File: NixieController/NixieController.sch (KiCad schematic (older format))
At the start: 87 parts, among them J1 Conn_02x05_Odd_Even, J10 Conn_01x06, J11 Conn_01x05, J12 Barrel_Jack, J13 Conn_02x05_Odd_Even, J14 Conn_02x05_Odd_Even, J15 Conn_02x05_Odd_Even, J16 Conn_01x07, J17 Conn_01x04, J18 Conn_01x02, J2 Conn_01x01, J3 Conn_01x01, J4 Conn_01x01, J5 Conn_01x01, J6 Conn_01x04, J8 Conn_01x04, Q1 2N2222A, Q2 2N2222A, Q3 2N2222A, Q4 2N2222A, SW1 SW_Push, SW2 SW_Push, SW3 SW_Push, U2 L7805

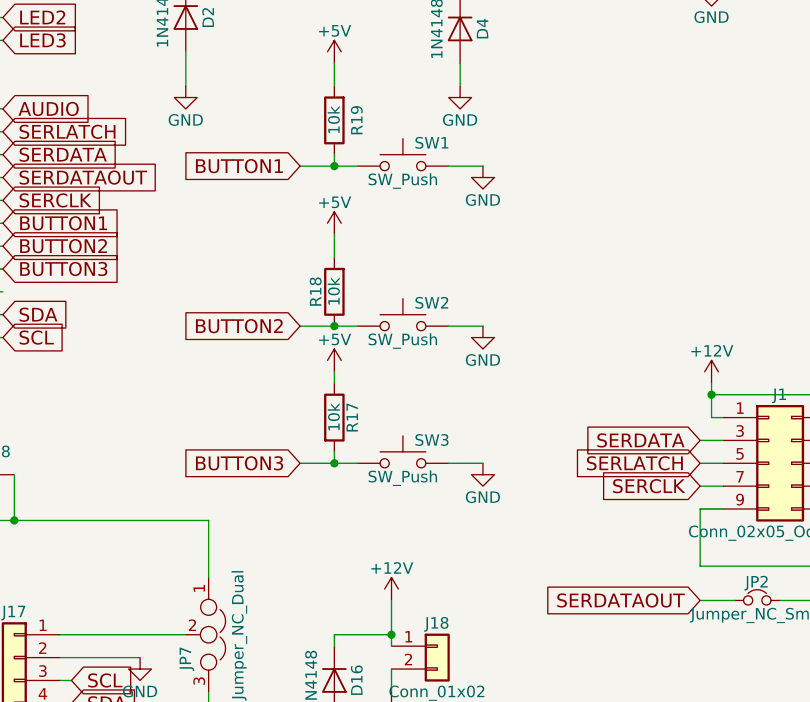
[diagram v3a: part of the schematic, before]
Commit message: Added capacitors to buttons to filter noise
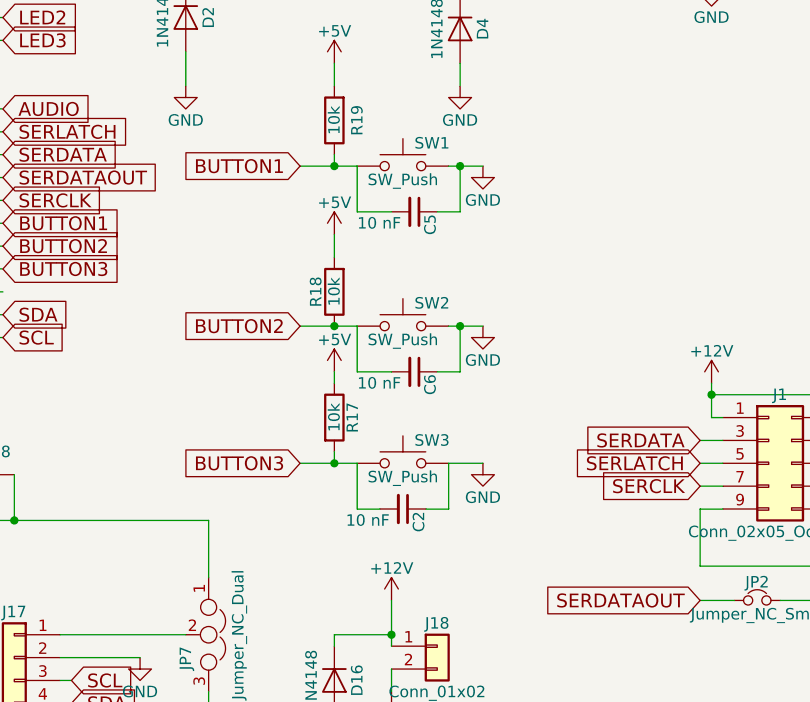
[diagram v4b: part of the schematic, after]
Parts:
- added C2, C5, C6: 10 nF, Capacitors_THT:C_Disc_D5.0mm_W2.5mm_P2.50mm, symbol C_Small
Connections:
- net BUTTON1: now also C5.2
- net BUTTON2: now also C6.2
- net BUTTON3: now also C2.2
- net GND: now also C2.1, C5.1, C6.1

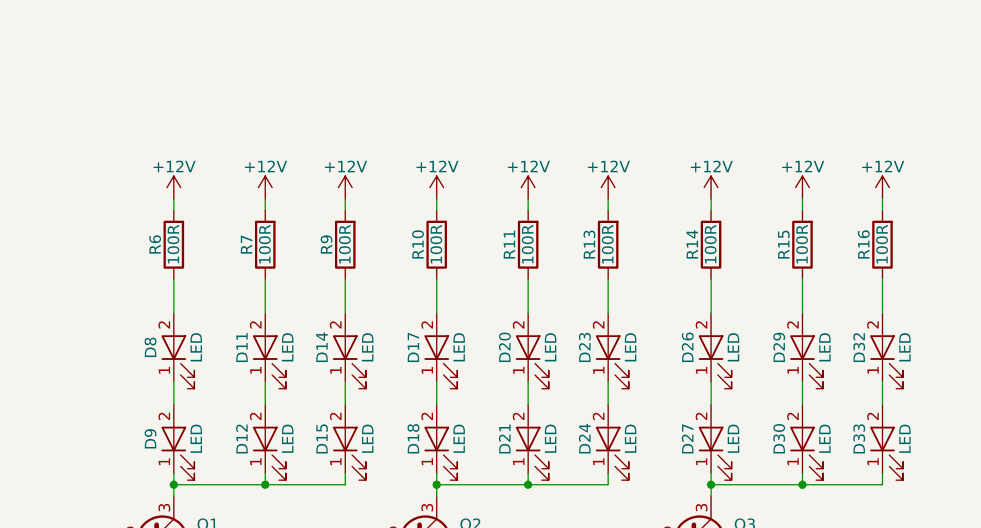
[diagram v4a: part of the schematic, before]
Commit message: Fixed slight error in schematic
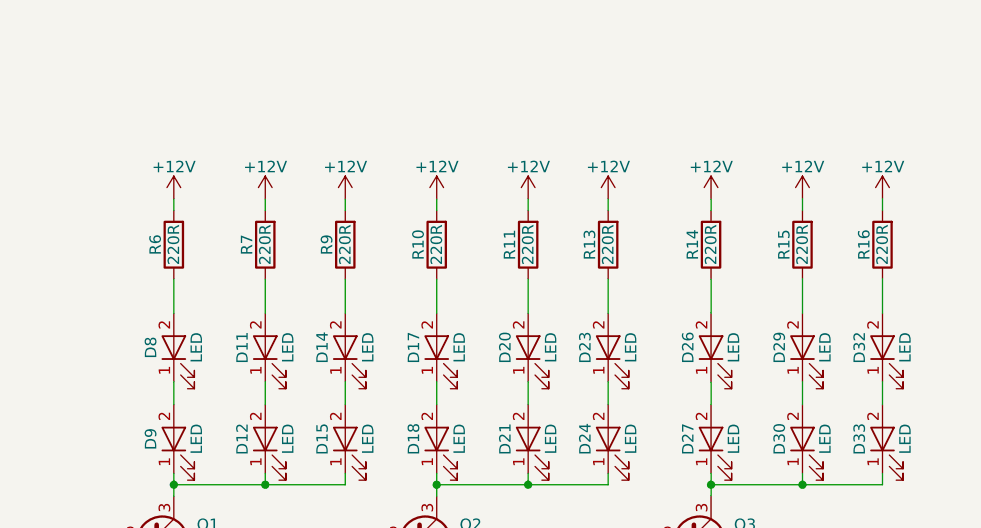
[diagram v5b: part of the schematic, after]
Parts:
- R10, R11, R13, R14, R15, R16, R6, R7, R9: value 100R -> 220R
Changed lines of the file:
@@
 P 7600 1700
 F 0 "R6" V 7680 1700 50  0000 C CNN
-F 1 "100R" V 7600 1700 50  0000 C CNN
+F 1 "220R" V 7600 1700 50  0000 C CNN
 F 2 "Resistors_THT:R_Axial_DIN0207_L6.3mm_D2.5mm_P7.62mm_Horizontal" V 7530 1700 50  0001 C CNN
 F 3 "" H 7600 1700 50  0001 C CNN
@@
 P 8000 1700
 F 0 "R7" V 8080 1700 50  0000 C CNN
-F 1 "100R" V 8000 1700 50  0000 C CNN
+F 1 "220R" V 8000 1700 50  0000 C CNN
 F 2 "Resistors_THT:R_Axial_DIN0207_L6.3mm_D2.5mm_P7.62mm_Horizontal" V 7930 1700 50  0001 C CNN
 F 3 "" H 8000 1700 50  0001 C CNN
@@
 P 8350 1700
 F 0 "R9" V 8430 1700 50  0000 C CNN
-F 1 "100R" V 8350 1700 50  0000 C CNN
+F 1 "220R" V 8350 1700 50  0000 C CNN
 F 2 "Resistors_THT:R_Axial_DIN0207_L6.3mm_D2.5mm_P7.62mm_Horizontal" V 8280 1700 50  0001 C CNN
 F 3 "" H 8350 1700 50  0001 C CNN
@@
 P 8750 1700
 F 0 "R10" V 8830 1700 50  0000 C CNN
-F 1 "100R" V 8750 1700 50  0000 C CNN
+F 1 "220R" V 8750 1700 50  0000 C CNN
 F 2 "Resistors_THT:R_Axial_DIN0207_L6.3mm_D2.5mm_P7.62mm_Horizontal" V 8680 1700 50  0001 C CNN
 F 3 "" H 8750 1700 50  0001 C CNN
@@
 P 9150 1700
 F 0 "R11" V 9230 1700 50  0000 C CNN
-F 1 "100R" V 9150 1700 50  0000 C CNN
+F 1 "220R" V 9150 1700 50  0000 C CNN
 F 2 "Resistors_THT:R_Axial_DIN0207_L6.3mm_D2.5mm_P7.62mm_Horizontal" V 9080 1700 50  0001 C CNN
 F 3 "" H 9150 1700 50  0001 C CNN
@@
 P 9500 1700
 F 0 "R13" V 9580 1700 50  0000 C CNN
-F 1 "100R" V 9500 1700 50  0000 C CNN
+F 1 "220R" V 9500 1700 50  0000 C CNN
 F 2 "Resistors_THT:R_Axial_DIN0207_L6.3mm_D2.5mm_P7.62mm_Horizontal" V 9430 1700 50  0001 C CNN
 F 3 "" H 9500 1700 50  0001 C CNN
@@
 P 9950 1700
 F 0 "R14" V 10030 1700 50  0000 C CNN
-F 1 "100R" V 9950 1700 50  0000 C CNN
+F 1 "220R" V 9950 1700 50  0000 C CNN
 F 2 "Resistors_THT:R_Axial_DIN0207_L6.3mm_D2.5mm_P7.62mm_Horizontal" V 9880 1700 50  0001 C CNN
 F 3 "" H 9950 1700 50  0001 C CNN
@@
 P 10350 1700
 F 0 "R15" V 10430 1700 50  0000 C CNN
-F 1 "100R" V 10350 1700 50  0000 C CNN
+F 1 "220R" V 10350 1700 50  0000 C CNN
 F 2 "Resistors_THT:R_Axial_DIN0207_L6.3mm_D2.5mm_P7.62mm_Horizontal" V 10280 1700 50  0001 C CNN
 F 3 "" H 10350 1700 50  0001 C CNN
@@
 P 10700 1700
 F 0 "R16" V 10780 1700 50  0000 C CNN
-F 1 "100R" V 10700 1700 50  0000 C CNN
+F 1 "220R" V 10700 1700 50  0000 C CNN
 F 2 "Resistors_THT:R_Axial_DIN0207_L6.3mm_D2.5mm_P7.62mm_Horizontal" V 10630 1700 50  0001 C CNN
 F 3 "" H 10700 1700 50  0001 C CNN
